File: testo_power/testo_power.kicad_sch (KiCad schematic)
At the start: 14 parts, among them J1 USB_C_Receptacle_PowerOnly_6P, J2 Conn_01x02_Socket, J3 Conn_01x02_Socket, Q2 IRLML6402TRPBF, U1 MCP73812

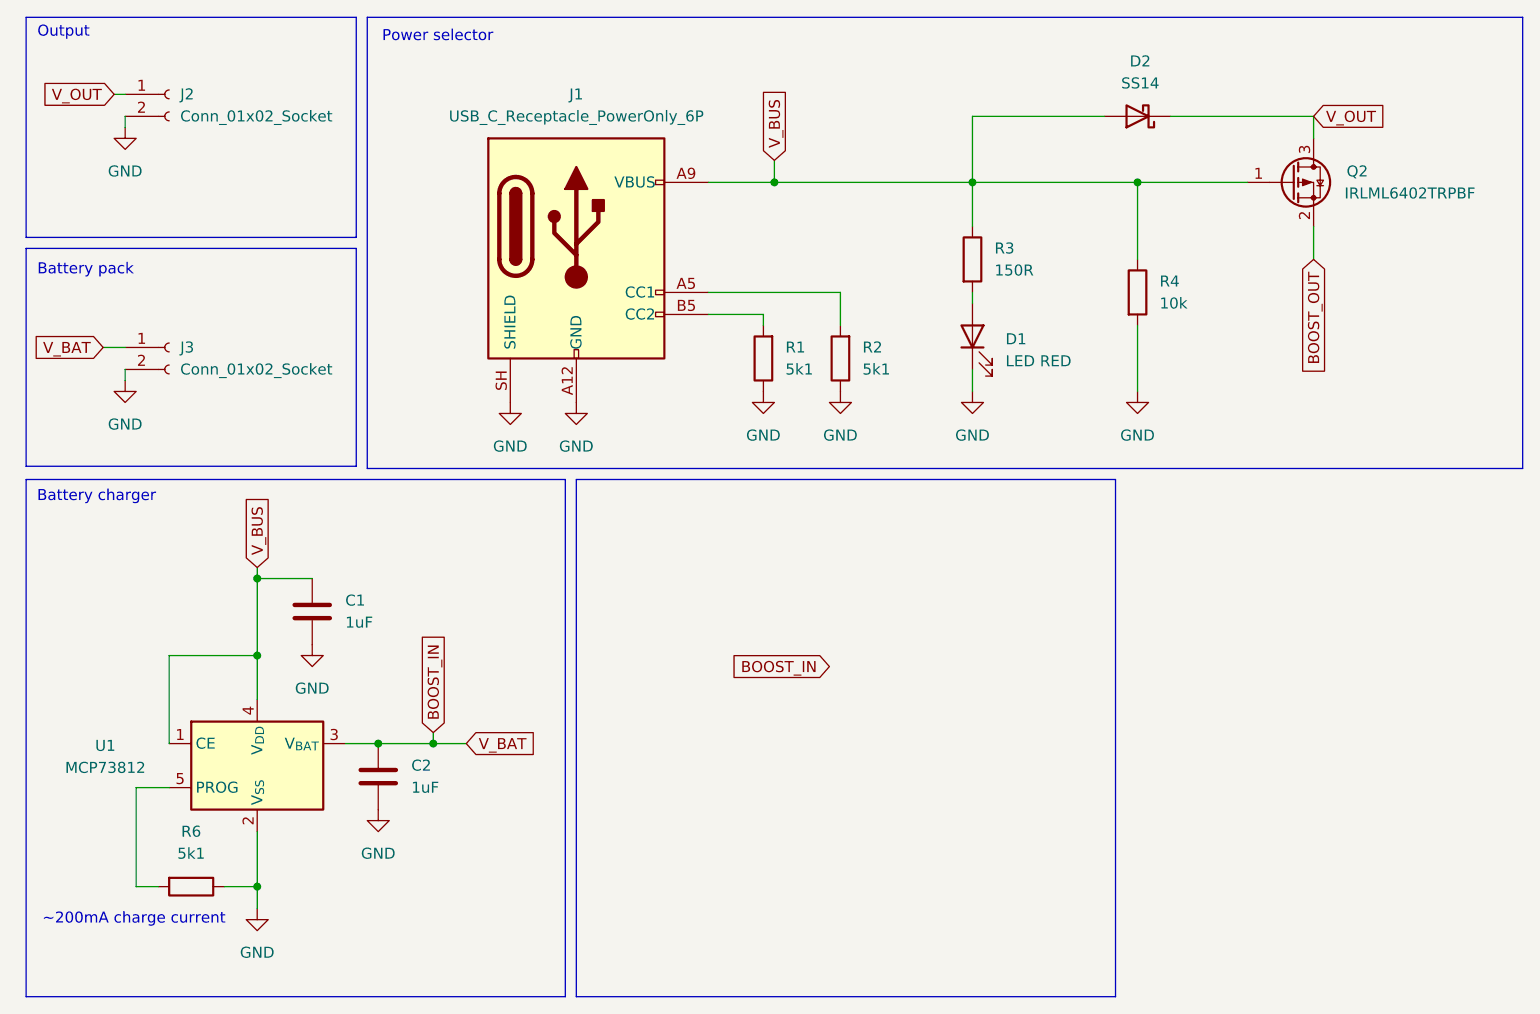
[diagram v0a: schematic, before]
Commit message: Added boost converter schematic
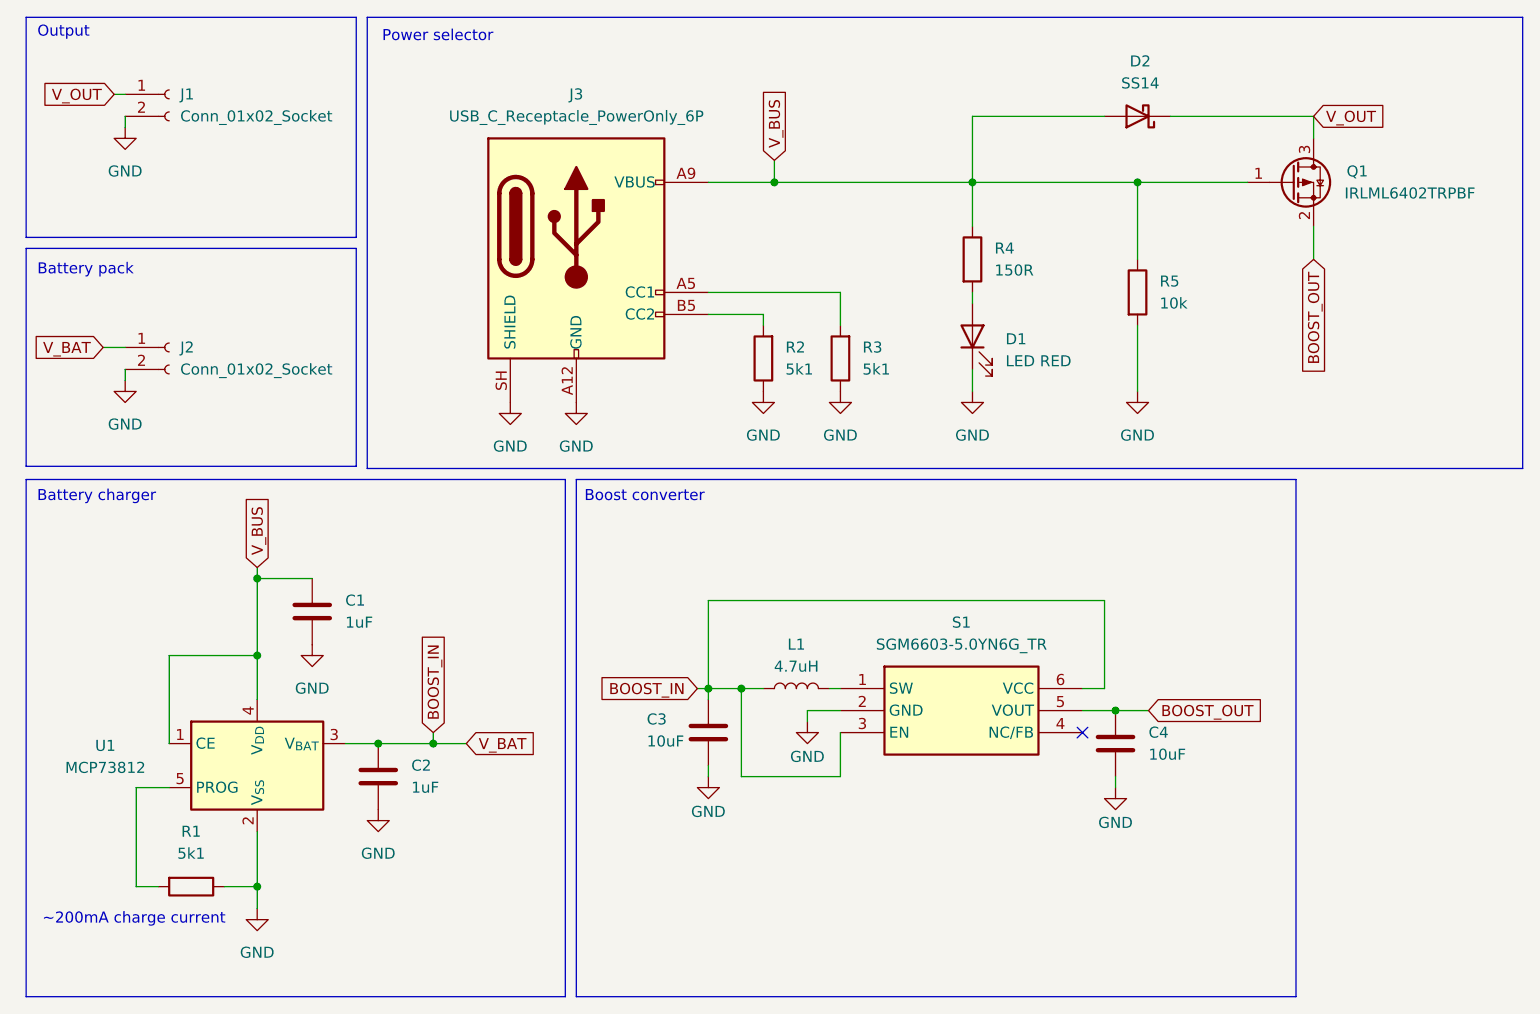
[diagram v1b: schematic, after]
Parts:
- added C3, C4: 10uF, symbol Device:C
- added L1: 4.7uH, symbol Device:L
- added S1: SGM6603-5.0YN6G_TR, SOT95P280X125-6N, symbol SamacSys_Parts:SGM6603-5.0YN6G_TR
- C1, C2: JLC Part# (none) -> C1592
- renumbered J2 to J1, J3 to J2, J1 to J3, Q2 to Q1, R6 to R1, R1 to R2, R2 to R3, R3 to R4, R4 to R5
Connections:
- net BOOST_IN: now also C3.1, L1.1, S1.3 (EN), S1.6 (VCC)
- net BOOST_OUT: now also C4.1, S1.5 (VOUT)
- net GND: now also C3.2, C4.2, S1.2 (GND)
- new net: L1.2, S1.1 (SW)
- no-connect marks 0 -> 1
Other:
- note added: "Boost converter"

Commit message: Added footprints
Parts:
- C1, C2, C3, C4: footprint (none) -> Capacitor_SMD:C_0603_1608Metric
- L1: footprint (none) -> Inductor_SMD:L_0805_2012Metric
- S1: footprint SOT95P280X125-6N -> SamacSys_Parts:SOT95P280X125-6N
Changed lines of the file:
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@@
 			)
 		)
-		(property "Footprint" ""
+		(property "Footprint" "Capacitor_SMD:C_0603_1608Metric"
 			(at 139.3952 100.33 0)
 			(hide yes)
@@
 			)
 		)
-		(property "Footprint" ""
+		(property "Footprint" "Capacitor_SMD:C_0603_1608Metric"
 			(at 92.4052 99.06 0)
 			(hide yes)
@@
 			)
 		)
-		(property "Footprint" "SOT95P280X125-6N"
+		(property "Footprint" "SamacSys_Parts:SOT95P280X125-6N"
 			(at 130.81 185.09 0)
 			(hide yes)
@@
 			)
 		)
-		(property "Footprint" ""
+		(property "Footprint" "Capacitor_SMD:C_0603_1608Metric"
 			(at 54.3052 104.14 0)
 			(hide yes)
@@
 			)
 		)
-		(property "Footprint" ""
+		(property "Footprint" "Capacitor_SMD:C_0603_1608Metric"
 			(at 46.6852 85.09 0)
 			(hide yes)
@@
 			)
 		)
-		(property "Footprint" ""
+		(property "Footprint" "Inductor_SMD:L_0805_2012Metric"
 			(at 101.6 90.17 0)
 			(hide yes)

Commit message: Replace molex connector
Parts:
- J1: now left out of the parts list
- J2: footprint Connector_Molex:Molex_CLIK-Mate_502382-0270_1x02-1MP_P1.25mm_Vertical -> SamacSys_Parts:0532610271; JLC Part# C27543 -> C225111
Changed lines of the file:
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@@
 		(body_style 1)
 		(exclude_from_sim no)
-		(in_bom yes)
-		(on_board yes)
+		(in_bom no)
+		(on_board no)
 		(in_pos_files yes)
 		(dnp no)
@@
 			)
 		)
-		(property "Footprint" "Connector_Molex:Molex_CLIK-Mate_502382-0270_1x02-1MP_P1.25mm_Vertical"
+		(property "Footprint" "SamacSys_Parts:0532610271"
 			(at 29.21 50.8 0)
 			(hide yes)
@@
 			)
 		)
-		(property "JLC Part#" "C27543"
+		(property "JLC Part#" "C225111"
 			(at 29.21 50.8 0)
 			(hide yes)

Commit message: Add production files for ordering
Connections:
- net GND: no longer J3.B12 (GND)
- net V_BUS: no longer J3.B9 (VBUS)
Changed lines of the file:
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@@
 		(pin "SH"
-		)
-		(pin "B12"
-		)
-		(pin "B9"
 		)
 		(pin "A5"
